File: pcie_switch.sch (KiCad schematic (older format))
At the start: 46 parts

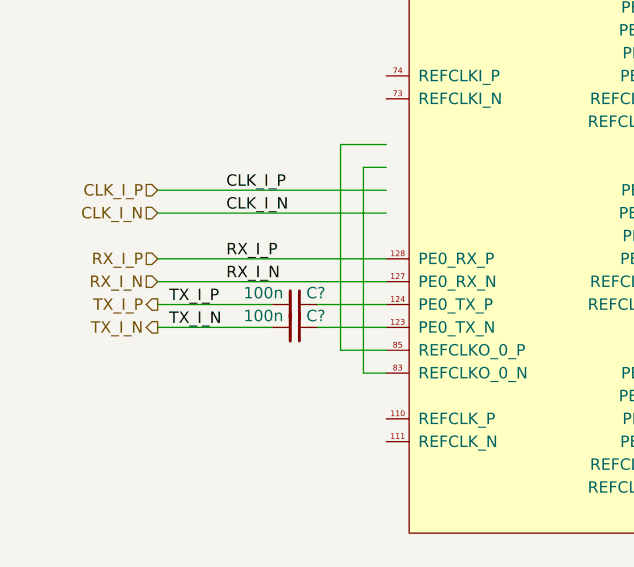
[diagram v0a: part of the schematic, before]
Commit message: sch: Move PHY blocks to main page
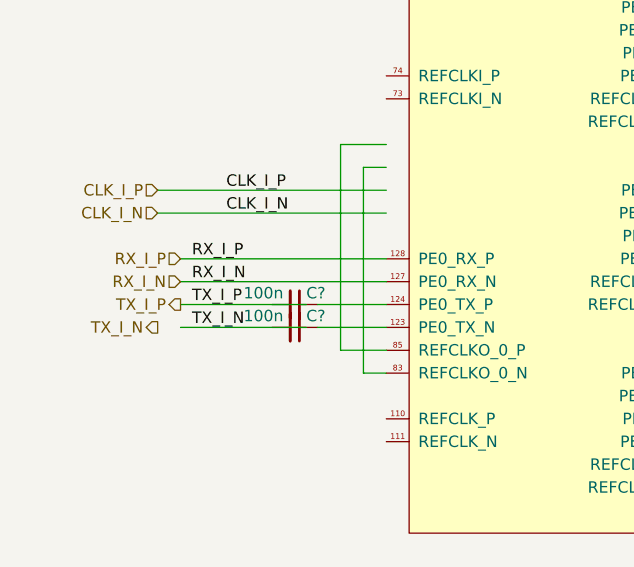
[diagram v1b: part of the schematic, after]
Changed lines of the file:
@@
 $Descr A4 11693 8268
 encoding utf-8
-Sheet 8 13
+Sheet 4 12
 Title "PCIe Switch"
 Date "2019-03-19"
@@
 $EndComp
 Wire Wire Line
-	2300 2600 1300 2600
-Text Label 1600 2600 0    50   ~ 0
+	2300 2600 1400 2600
+Text Label 1450 2600 0    50   ~ 0
 RX_I_P
 Wire Wire Line
-	2300 2700 1300 2700
-Text Label 1600 2700 0    50   ~ 0
+	2300 2700 1400 2700
+Text Label 1450 2700 0    50   ~ 0
 RX_I_N
 Wire Wire Line
-	1800 2800 1300 2800
-Text Label 1350 2800 0    50   ~ 0
+	1950 2800 1400 2800
+Text Label 1450 2800 0    50   ~ 0
 TX_I_P
 Wire Wire Line
-	1800 2900 1300 2900
-Text Label 1350 2900 0    50   ~ 0
+	1950 2900 1400 2900
+Text Label 1450 2900 0    50   ~ 0
 TX_I_N
-Text HLabel 1300 2600 0    50   Input ~ 0
+Text HLabel 1400 2600 0    50   Input ~ 0
 RX_I_P
-Text HLabel 1300 2700 0    50   Input ~ 0
+Text HLabel 1400 2700 0    50   Input ~ 0
 RX_I_N
-Text HLabel 1300 2800 0    50   Output ~ 0
+Text HLabel 1400 2800 0    50   Output ~ 0
 TX_I_P
 Text HLabel 1300 2900 0    50   Output ~ 0

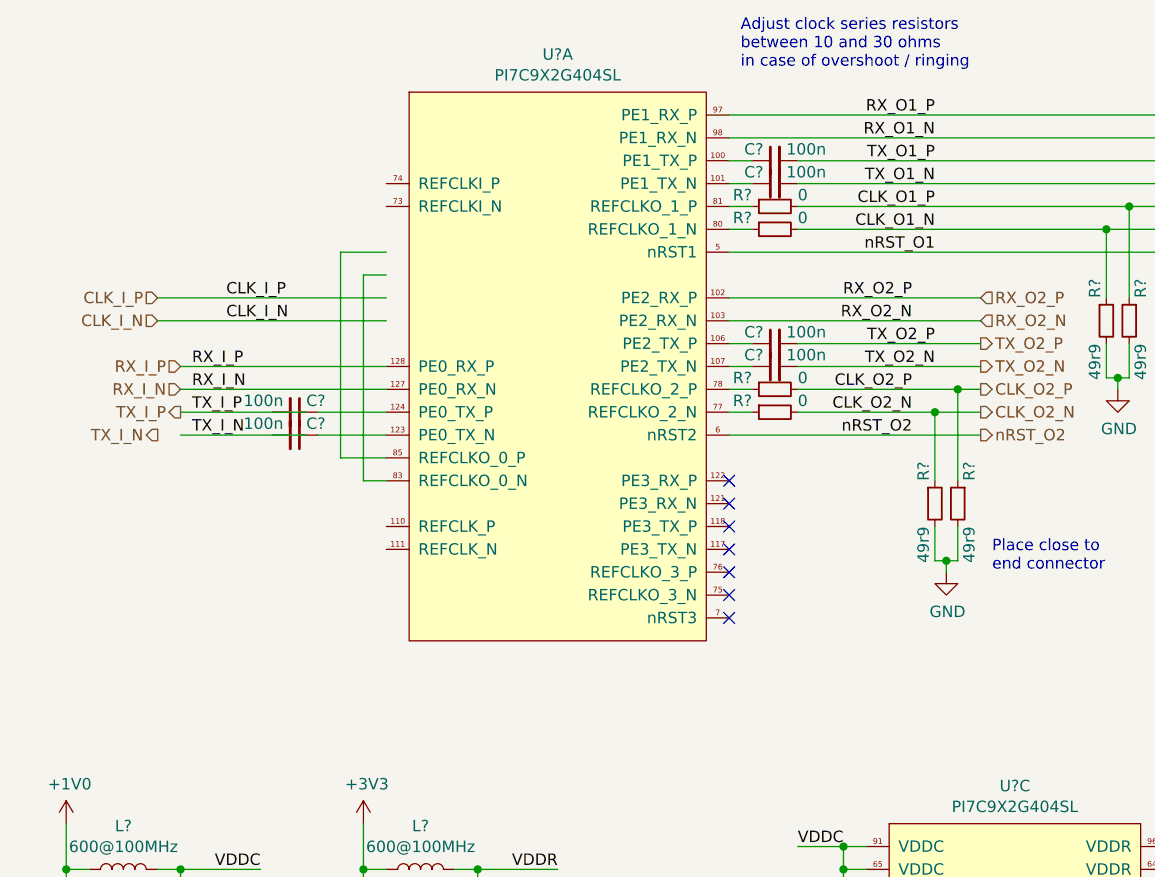
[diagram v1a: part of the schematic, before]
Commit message: sch: Better PCIe clock terminations
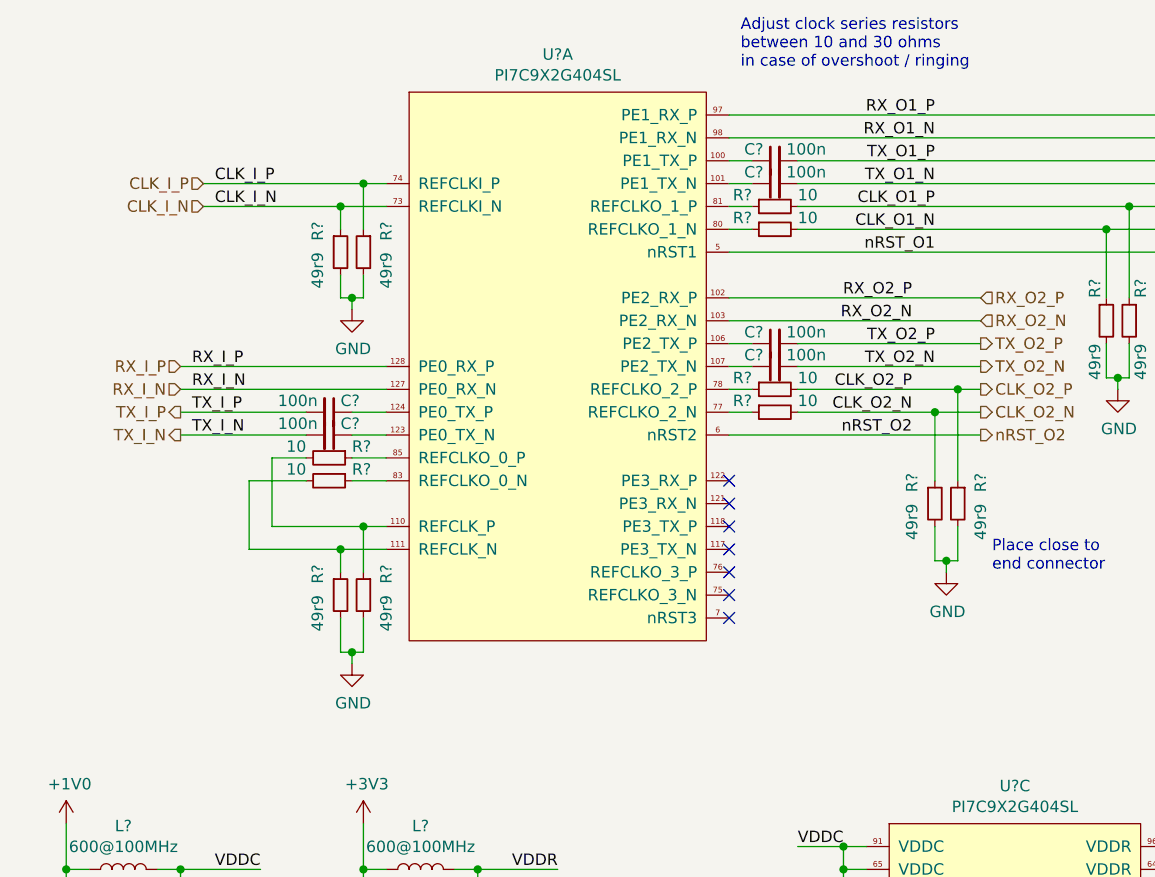
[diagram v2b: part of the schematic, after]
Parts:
- added R? (x2): 10, symbol Device:R_Small
- added R? (x4): 49r9, symbol Device:R_Small
- R? (x4): value 0 -> 10
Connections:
- wire segments 246 -> 266
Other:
- moved on the sheet: C?

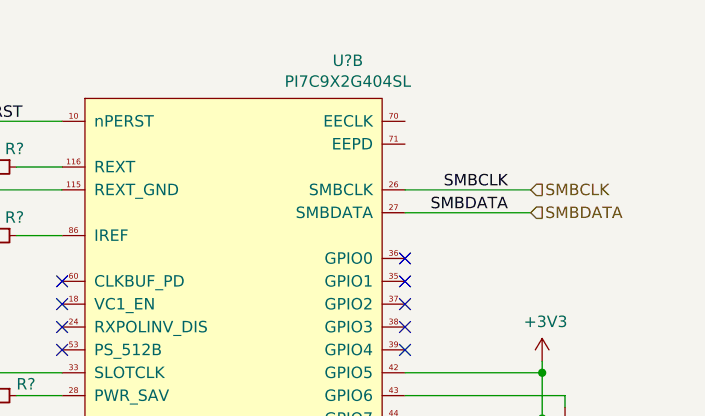
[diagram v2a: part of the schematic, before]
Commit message: sch: Misc fixes
- add missing NC on PCIe switch
- fix incorrect cap values on PCIe supply
- fix main schematic interco labels
- fix PHY JTAG signal name
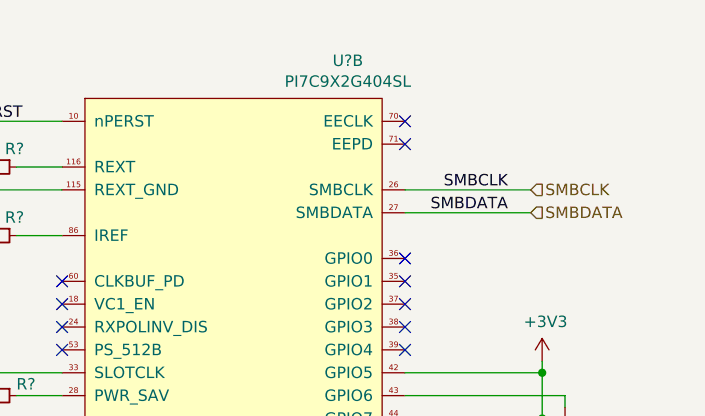
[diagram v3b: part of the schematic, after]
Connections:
- no-connect marks 25 -> 27
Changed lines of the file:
@@
 	0    -1   1    0
 $EndComp
+NoConn ~ 9500 1500
+NoConn ~ 9500 1600
 $EndSCHEMATC

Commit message: sch: Add PCIe switch clocks documentation
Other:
- note added: "The PI7C9X2G404SL has an integrated clock buffer and\nfan-out, whose input is REFCLK_I. Yet it still needs a\nreference clock to work. Thus we feed it one of its clock\noutput (REFCLKO_0) to its reference clock input (REFCLK)."
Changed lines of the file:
@@
 NoConn ~ 9500 1500
 NoConn ~ 9500 1600
+Text Notes 750  1100 0    50   ~ 0
+The PI7C9X2G404SL has an integrated clock buffer and\nfan-out, whose input is REFCLK_I. Yet it still needs a\nreference clock to work. Thus we feed it one of its clock\noutput (REFCLKO_0) to its reference clock input (REFCLK).
 $EndSCHEMATC

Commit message: sch: Make ERC happy with dummy power outputs
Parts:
- added DS? (x6): DummySupply, symbol pimouss-motherboard:DummySupply
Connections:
- net AVDD: now also DS?.~ (Dummy)
- net AVDDH: now also DS?.~ (Dummy)
- net CVDDR: now also DS?.~ (Dummy)
- net VDDC: now also DS?.~ (Dummy)
- net VDDCAUX: now also DS?.~ (Dummy)
- net VDDR: now also DS?.~ (Dummy)
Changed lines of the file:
@@
 	0    -1   1    0
 $EndComp
-NoConn ~ 9500 1500
-NoConn ~ 9500 1600
+NoConn ~ 9500 1750
+NoConn ~ 9500 1850
 Text Notes 750  1100 0    50   ~ 0
 The PI7C9X2G404SL has an integrated clock buffer and\nfan-out, whose input is REFCLK_I. Yet it still needs a\nreference clock to work. Thus we feed it one of its clock\noutput (REFCLKO_0) to its reference clock input (REFCLK).
+$Comp
+L pimouss-motherboard:DummySupply DS?
+U 1 1 5E03E9D7
+P 1400 4800
+AR Path="/5D0C4621/5E03E9D7" Ref="DS?"  Part="1"
+AR Path="/5D05A5E3/5E03E9D7" Ref="DS?"  Part="1"
+AR Path="/5E03E9D7" Ref="DS?"  Part="1"
+AR Path="/5C91A44F/5D5418D5/5E03E9D7" Ref="DS?"  Part="1"
+F 0 "DS?" H 1400 4800 50  0001 C CNN
+F 1 "DummySupply" H 1400 4800 50  0001 C CNN
+F 2 "" H 1400 4800 50  0001 C CNN
+F 3 "" H 1400 4800 50  0001 C CNN
+	1    1400 4800
+	1    0    0    -1
+$EndComp
+$Comp
+L pimouss-motherboard:DummySupply DS?
+U 1 1 5E407473
+P 1400 5900
+AR Path="/5D0C4621/5E407473" Ref="DS?"  Part="1"
+AR Path="/5D05A5E3/5E407473" Ref="DS?"  Part="1"
+AR Path="/5E407473" Ref="DS?"  Part="1"
+AR Path="/5C91A44F/5D5418D5/5E407473" Ref="DS?"  Part="1"
+F 0 "DS?" H 1400 5900 50  0001 C CNN
+F 1 "DummySupply" H 1400 5900 50  0001 C CNN
+F 2 "" H 1400 5900 50  0001 C CNN
+F 3 "" H 1400 5900 50  0001 C CNN
+	1    1400 5900
+	1    0    0    -1
+$EndComp
+$Comp
+L pimouss-motherboard:DummySupply DS?
+U 1 1 5E407C3E
+P 1400 7000
+AR Path="/5D0C4621/5E407C3E" Ref="DS?"  Part="1"
+AR Path="/5D05A5E3/5E407C3E" Ref="DS?"  Part="1"
+AR Path="/5E407C3E" Ref="DS?"  Part="1"
+AR Path="/5C91A44F/5D5418D5/5E407C3E" Ref="DS?"  Part="1"
+F 0 "DS?" H 1400 7000 50  0001 C CNN
+F 1 "DummySupply" H 1400 7000 50  0001 C CNN
+F 2 "" H 1400 7000 50  0001 C CNN
+F 3 "" H 1400 7000 50  0001 C CNN
+	1    1400 7000
+	1    0    0    -1
+$EndComp
+$Comp
+L pimouss-motherboard:DummySupply DS?
+U 1 1 5E40880E
+P 2700 6900
+AR Path="/5D0C4621/5E40880E" Ref="DS?"  Part="1"
+AR Path="/5D05A5E3/5E40880E" Ref="DS?"  Part="1"
+AR Path="/5E40880E" Ref="DS?"  Part="1"
+AR Path="/5C91A44F/5D5418D5/5E40880E" Ref="DS?"  Part="1"
+F 0 "DS?" H 2700 6900 50  0001 C CNN
+F 1 "DummySupply" H 2700 6900 50  0001 C CNN
+F 2 "" H 2700 6900 50  0001 C CNN
+F 3 "" H 2700 6900 50  0001 C CNN
+	1    2700 6900
+	1    0    0    -1
+$EndComp
+Connection ~ 2700 6900
+$Comp
+L pimouss-motherboard:DummySupply DS?
+U 1 1 5E40910D
+P 2700 5900
+AR Path="/5D0C4621/5E40910D" Ref="DS?"  Part="1"
+AR Path="/5D05A5E3/5E40910D" Ref="DS?"  Part="1"
+AR Path="/5E40910D" Ref="DS?"  Part="1"
+AR Path="/5C91A44F/5D5418D5/5E40910D" Ref="DS?"  Part="1"
+F 0 "DS?" H 2700 5900 50  0001 C CNN
+F 1 "DummySupply" H 2700 5900 50  0001 C CNN
+F 2 "" H 2700 5900 50  0001 C CNN
+F 3 "" H 2700 5900 50  0001 C CNN
+	1    2700 5900
+	1    0    0    -1
+$EndComp
+$Comp
+L pimouss-motherboard:DummySupply DS?
+U 1 1 5E409AA0
+P 2700 4800
+AR Path="/5D0C4621/5E409AA0" Ref="DS?"  Part="1"
+AR Path="/5D05A5E3/5E409AA0" Ref="DS?"  Part="1"
+AR Path="/5E409AA0" Ref="DS?"  Part="1"
+AR Path="/5C91A44F/5D5418D5/5E409AA0" Ref="DS?"  Part="1"
+F 0 "DS?" H 2700 4800 50  0001 C CNN
+F 1 "DummySupply" H 2700 4800 50  0001 C CNN
+F 2 "" H 2700 4800 50  0001 C CNN
+F 3 "" H 2700 4800 50  0001 C CNN
+	1    2700 4800
+	1    0    0    -1
+$EndComp
 $EndSCHEMATC

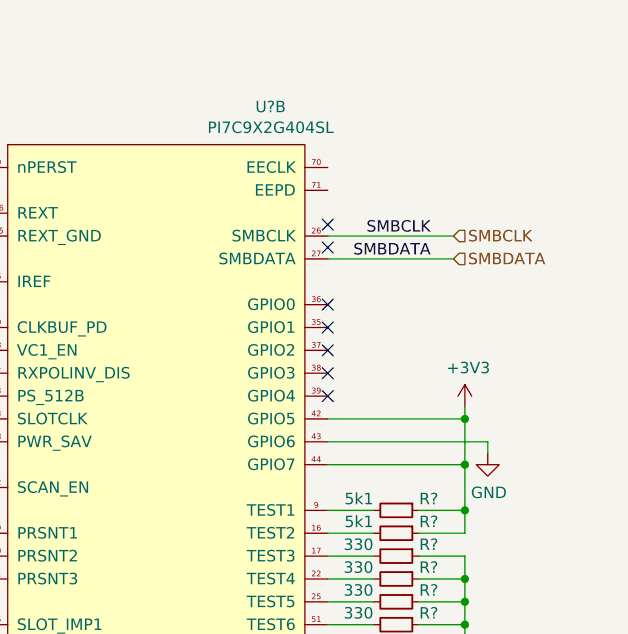
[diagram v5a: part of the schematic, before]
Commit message: lib, sch: Misc changes to make ERC happy
- add resistors to PCIe switch GPIOs
- add NC flags on PHY unused LED outputs
- add dummy supply on Earth PSU
- add dummy supply on PHY ref clock's VCC
- LTC3633: deduplicate SW1/2 outputs
- ILS8033: deduplicate LX1/2 and PGND1/2 outputs
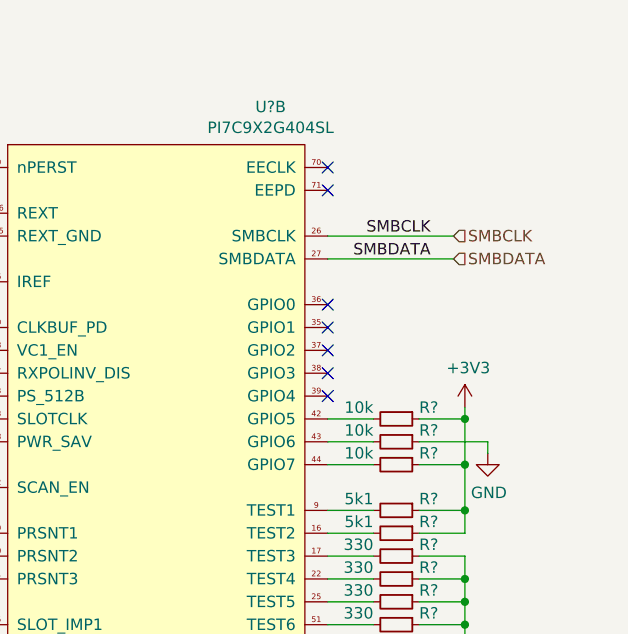
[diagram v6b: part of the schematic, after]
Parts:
- added R? (x3): 10k, symbol Device:R_Small
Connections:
- net +3V3: now also R?.1, R?.1; no longer U?.42 (GPIO5), U?.44 (GPIO7)
- net GND: now also R?.1; no longer U?.43 (GPIO6)
- new net: R?.2, U?.42 (GPIO5)
- new net: R?.2, U?.43 (GPIO6)
- new net: R?.2, U?.44 (GPIO7)
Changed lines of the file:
@@
 NoConn ~ 9500 2400
 NoConn ~ 9500 2500
-Wire Wire Line
-	10100 2550 10100 2600
-Wire Wire Line
-	9500 2600 10100 2600
-Connection ~ 10100 2600
-Wire Wire Line
-	10100 2600 10100 2800
-Wire Wire Line
-	9500 2800 10100 2800
-Connection ~ 10100 2800
-Wire Wire Line
-	10100 2800 10100 3000
 $Comp
 L power:GND #PWR?
@@
 	1    0    0    -1
 $EndComp
-Wire Wire Line
-	9500 2700 10200 2700
 Wire Wire Line
 	10200 2700 10200 2750
@@
 	0    -1   1    0
 $EndComp
-NoConn ~ 9500 1750
-NoConn ~ 9500 1850
 Text Notes 750  1100 0    50   ~ 0
 The PI7C9X2G404SL has an integrated clock buffer and\nfan-out, whose input is REFCLK_I. Yet it still needs a\nreference clock to work. Thus we feed it one of its clock\noutput (REFCLKO_0) to its reference clock input (REFCLK).
@@
 	1    0    0    -1
 $EndComp
+Wire Wire Line
+	10100 2550 10100 2600
+$Comp
+L Device:R_Small R?
+U 1 1 5E506E4F
+P 9800 2600
+F 0 "R?" V 9750 2700 50  0000 L CNN
+F 1 "10k" V 9750 2500 50  0000 R CNN
+F 2 "" H 9800 2600 50  0001 C CNN
+F 3 "~" H 9800 2600 50  0001 C CNN
+	1    9800 2600
+	0    1    1    0
+$EndComp
+$Comp
+L Device:R_Small R?
+U 1 1 5E531554
+P 9800 2700
+F 0 "R?" V 9750 2800 50  0000 L CNN
+F 1 "10k" V 9750 2600 50  0000 R CNN
+F 2 "" H 9800 2700 50  0001 C CNN
+F 3 "~" H 9800 2700 50  0001 C CNN
+	1    9800 2700
+	0    1    1    0
+$EndComp
+$Comp
+L Device:R_Small R?
+U 1 1 5E531846
+P 9800 2800
+F 0 "R?" V 9750 2900 50  0000 L CNN
+F 1 "10k" V 9750 2700 50  0000 R CNN
+F 2 "" H 9800 2800 50  0001 C CNN
+F 3 "~" H 9800 2800 50  0001 C CNN
+	1    9800 2800
+	0    1    1    0
+$EndComp
+Wire Wire Line
+	9500 2600 9700 2600
+Wire Wire Line
+	9700 2700 9500 2700
+Wire Wire Line
+	9500 2800 9700 2800
+Wire Wire Line
+	9900 2600 10100 2600
+Connection ~ 10100 2600
+Wire Wire Line
+	10100 2600 10100 2800
+Wire Wire Line
+	9900 2700 10200 2700
+Wire Wire Line
+	9900 2800 10100 2800
+Connection ~ 10100 2800
+Wire Wire Line
+	10100 2800 10100 3000
+NoConn ~ 9500 1500
+NoConn ~ 9500 1600
 $EndSCHEMATC
